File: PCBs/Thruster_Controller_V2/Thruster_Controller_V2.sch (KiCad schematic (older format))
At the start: 33 parts, among them J1 PHASE_A, J2 PHASE_B, J3 PHASE_C, J4 Conn_01x01, J5 Pogo Conn, J6 Conn_01x01, J7 Conn_01x01, J8 Conn_01x01, U4 TPS62172DSGR, U8 MCP2562, Y1 20MHz

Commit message: Powertrain Schematic
- Updated PT schematic, footprints, and part numbers.
- Big change is moving from the DRV8305 to the DRV8320S
- BIG space and cost savings!!
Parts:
- removed C21, C22: 15pF, Capacitors_SMD:C_0402, symbol Device:C_Small
- removed C29: 1uF, Capacitors_SMD:C_0603, symbol Device:C_Small
- removed C30, C42: 0.1uF, Capacitors_SMD:C_0402, symbol Device:C_Small
- removed C49: 10uF, Capacitors_SMD:C_0805, symbol Device:C_Small
- removed C50: 22uF, Capacitors_SMD:C_0805, symbol Device:C_Small
- removed H1, H2: MountingHole, Thruster_Controller:MountingHole_M2, symbol Mechanical:MountingHole
- removed L1: 2.2uH, Inductors_SMD:L_0805, symbol Device:L_Small
- removed R17: 10k, Resistors_SMD:R_0402, symbol Device:R_Small_US
- removed R23: 100k, Resistors_SMD:R_0402_NoSilk, symbol Device:R_Small_US
- removed TP2: TestPoint, Thruster_Controller:TestPoint_Pad_D1.0mm, symbol Connector:TestPoint
- removed U4: TPS62172DSGR, Thruster_Controller:8-Pin_WSON, symbol Thruster_Controller:TPS62172DSGR
- removed Y1: 20MHz, Crystals:Crystal_SMD_SeikoEpson_TSX3225-4pin_3.2x2.5mm, symbol Device:Crystal_GND24
- added C?: 1uF, Capacitors_SMD:C_0603, symbol Device:C_Small
- added C?: 1uF, Capacitors_SMD:C_0805, symbol Device:C_Small
- added U?: NCP718AMT330, Housings_DFN_QFN:DFN-6-1EP_2x2mm_Pitch0.65mm, symbol Thruster_Controller:NCP718AMT330
- R19: footprint Resistors_SMD:R_0805 -> Resistors_SMD:R_0603; Digikey 2019-RK73B2ATTD331JCT-ND -> RMCF0603JT330RCT-ND
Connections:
- net labels removed: +5V
- wire segments 156 -> 99
- no-connect marks 1 -> 0
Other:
- note added: "3.3V Linear Regulator"
- note removed: "3.3V Regulator"
- note removed: "CAN chips decoupling cap"
- moved on the sheet: C23, C28, D1, D3, J4, J6, R19, R35, R7, TP1, TP3, U8

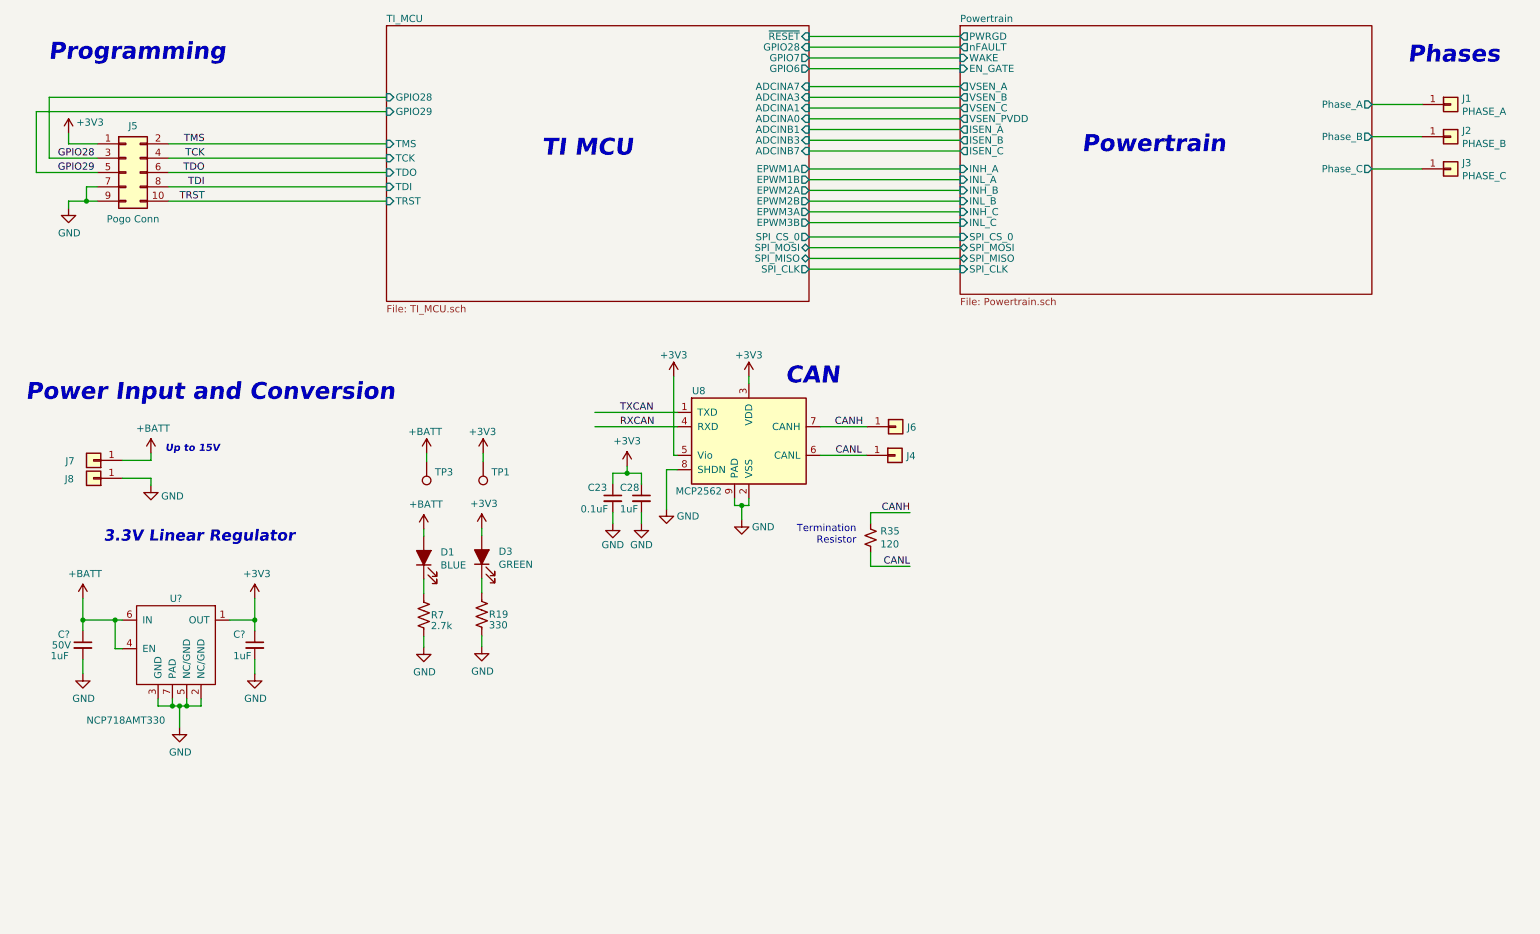
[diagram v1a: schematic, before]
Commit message: Schematic V1
- Completed New Schematic
_ Multiplexed all required signals, may need to redo some arrangments to aid in routing, just because I can and already have to reassign all pins in the SW.
- Created new BOM, only $1 more expensive per board, still might be able to lower that further.
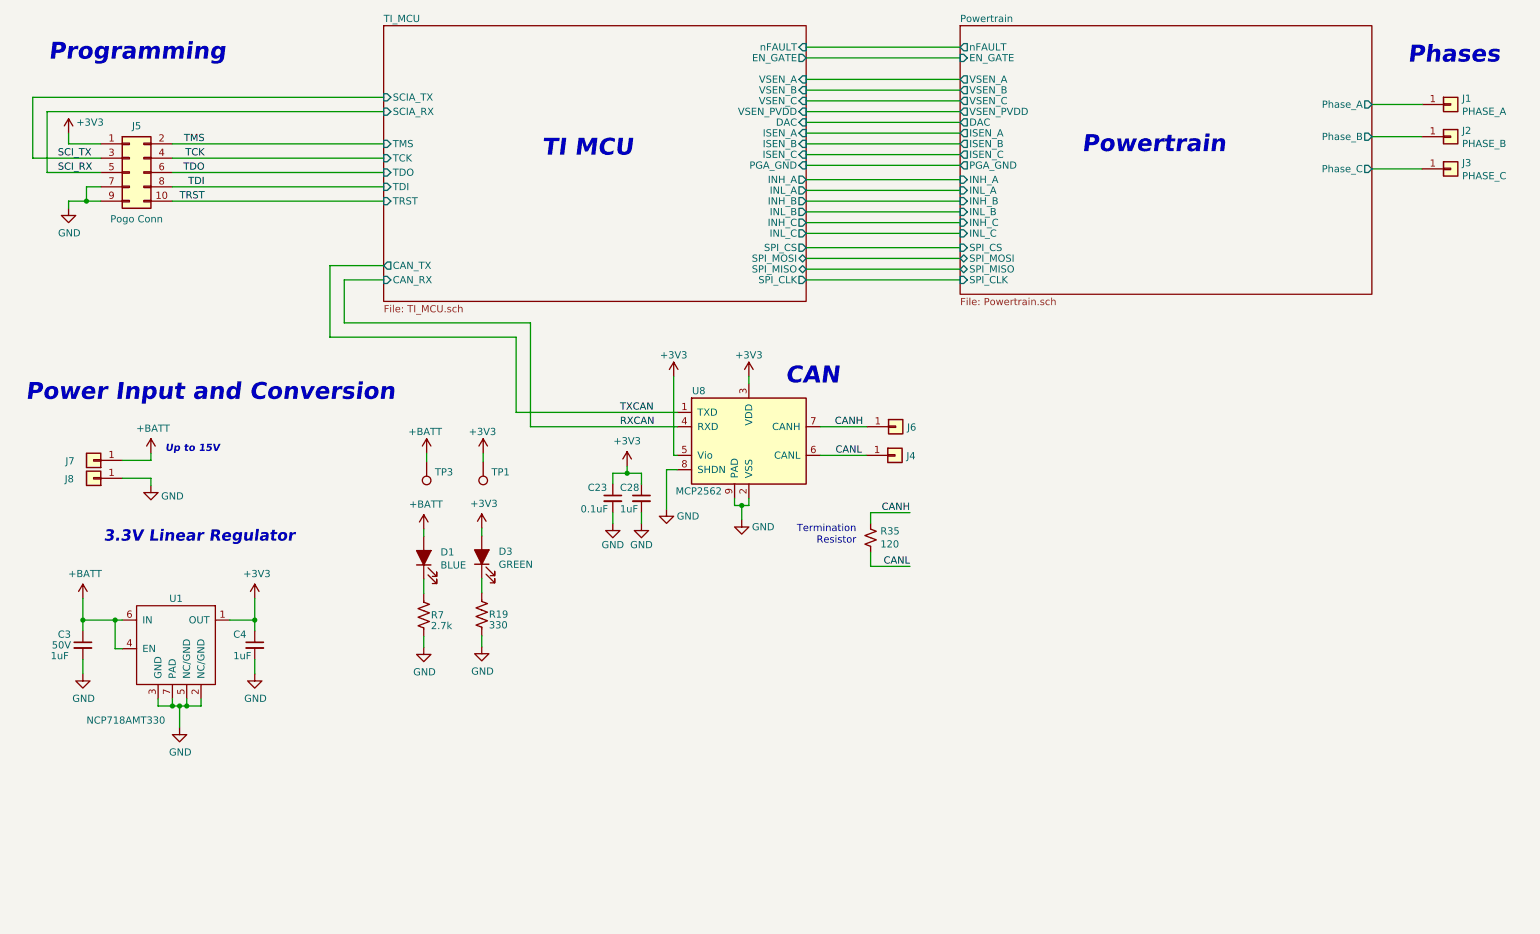
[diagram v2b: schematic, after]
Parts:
- gave numbers to parts that had none: 3
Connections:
- net GPIO28 renamed SCI_TX
- net GPIO29 renamed SCI_RX
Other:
- moved on the sheet: J5

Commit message: Schematic Work / BOM
- Double checking pinout
- Adding digikey PNs for all components, cannot do a mouser run for a small quantity (1-2 boards)
- Generated BOM
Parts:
- R19: value 330 -> 180; Digikey RMCF0603JT330RCT-ND -> 2019-RK73B1JTTD181JCT-ND
- U1: Digikey (none) -> NCP718AMT330TBGOSCT-ND
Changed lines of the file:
@@
 Sheet 1 3
 Title "FOC Thruster Controller "
-Date "2020-05-04"
+Date "2020-08-22"
 Rev "V2"
 Comp "Mark Belbin"
@@
 Text Notes 10300 1725 0    118  Italic 24
 Phases
-Text Notes 1195 5065 0    79   Italic 16
+Text Notes 1050 5125 0    79   Italic 16
 3.3V Linear Regulator
 Wire Wire Line
@@
 F 2 "Housings_DFN_QFN:DFN-6-1EP_2x2mm_Pitch0.65mm" H 1675 5600 50  0001 C CNN
 F 3 "https://www.mouser.ca/datasheet/2/308/NCP718-D-1224359.pdf" H 1625 5400 50  0001 C CNN
-F 4 "" H 1675 5750 50  0001 C CNN "Digikey"
+F 4 "NCP718AMT330TBGOSCT-ND" H 1675 5750 50  0001 C CNN "Digikey"
 F 5 "863-NCP718AMT330TBG" H 1675 5750 50  0001 C CNN "Mouser"
 	1    1675 5750
@@
 AR Path="/5E5672C2" Ref="R19"  Part="1"
 F 0 "R19" H 3885 5560 50  0000 L CNN
-F 1 "330" H 3885 5485 50  0000 L CNN
+F 1 "180" H 3885 5485 50  0000 L CNN
 F 2 "Resistors_SMD:R_0603" V 3875 5550 50  0001 C CNN
 F 3 "~" H 3835 5560 50  0001 C CNN
-F 4 "RMCF0603JT330RCT-ND" H 3835 5560 50  0001 C CNN "Digikey"
+F 4 "2019-RK73B1JTTD181JCT-ND" H 3835 5560 50  0001 C CNN "Digikey"
 	1    3835 5560
 	1    0    0    -1

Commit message: 3V3 LED
- Decreased in series resistor to 100 ohms from 180
- This increased brightness of the LED nicely, which is important to get through clear epoxy.
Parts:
- R19: value 180 -> 100; Digikey 2019-RK73B1JTTD181JCT-ND -> 2019-RK73B1JTTD101JCT-ND
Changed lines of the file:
@@
 AR Path="/5E5672C2" Ref="R19"  Part="1"
 F 0 "R19" H 3885 5560 50  0000 L CNN
-F 1 "180" H 3885 5485 50  0000 L CNN
+F 1 "100" H 3885 5485 50  0000 L CNN
 F 2 "Resistors_SMD:R_0603" V 3875 5550 50  0001 C CNN
 F 3 "~" H 3835 5560 50  0001 C CNN
-F 4 "2019-RK73B1JTTD181JCT-ND" H 3835 5560 50  0001 C CNN "Digikey"
+F 4 "2019-RK73B1JTTD101JCT-ND" H 3835 5560 50  0001 C CNN "Digikey"
 	1    3835 5560
 	1    0    0    -1

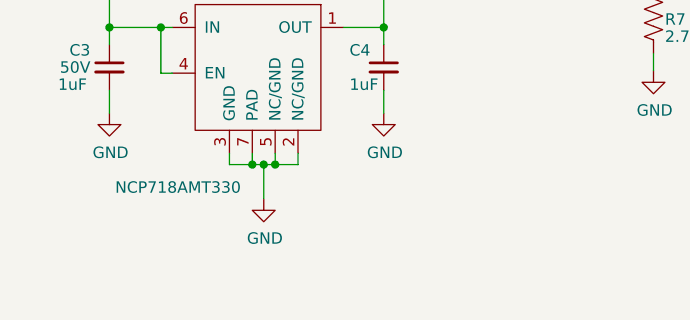
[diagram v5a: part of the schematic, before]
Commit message: Started CAN updates
- Need to fix CAN transciever, add 5V rail!
- Also subbing in a new transciever that is a newer PN and is lower in cost.
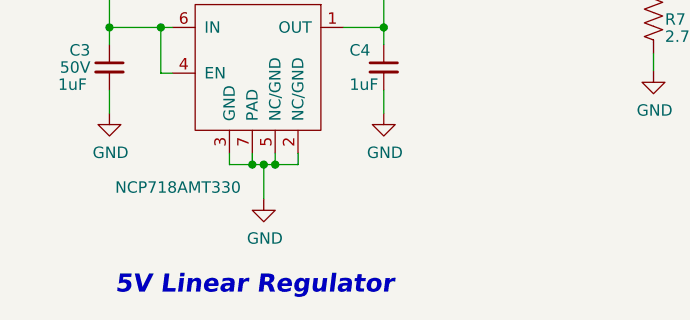
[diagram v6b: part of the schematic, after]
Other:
- note added: "5V Linear Regulator"
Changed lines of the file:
@@
 Wire Wire Line
 	4175 4250 5200 4250
+Text Notes 1075 6775 0    79   Italic 16
+5V Linear Regulator
 $EndSCHEMATC

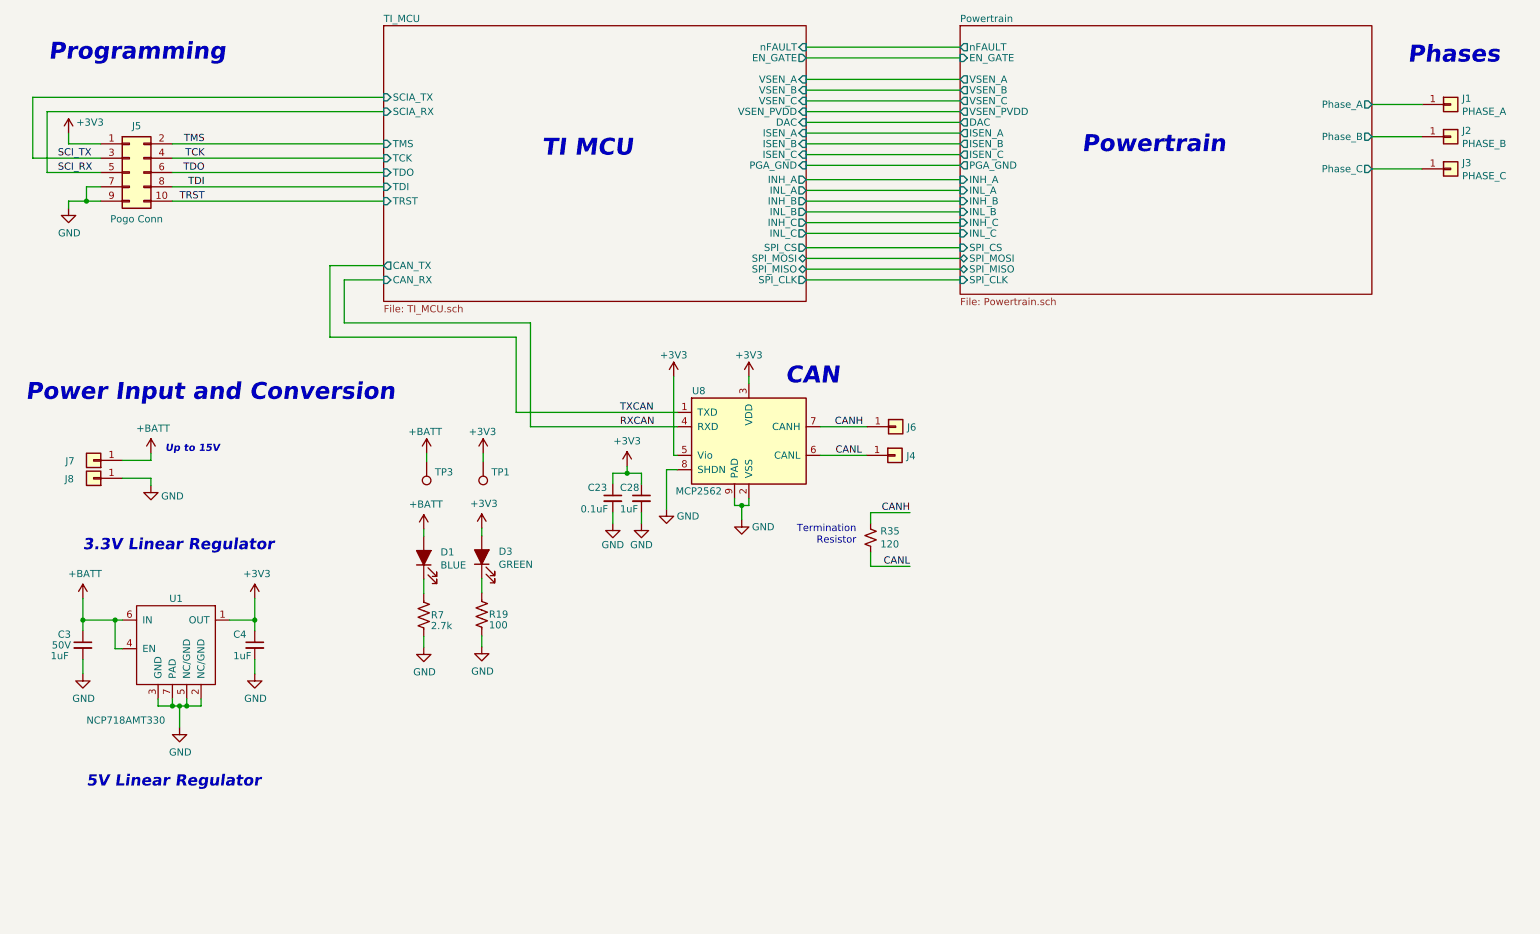
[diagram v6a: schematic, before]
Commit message: Schematic Changes
- Added 5V LDO
- Added 5V LED indicator
- Added 5V testpad
- Changed CAN Transciever to a cheaper and newer model.
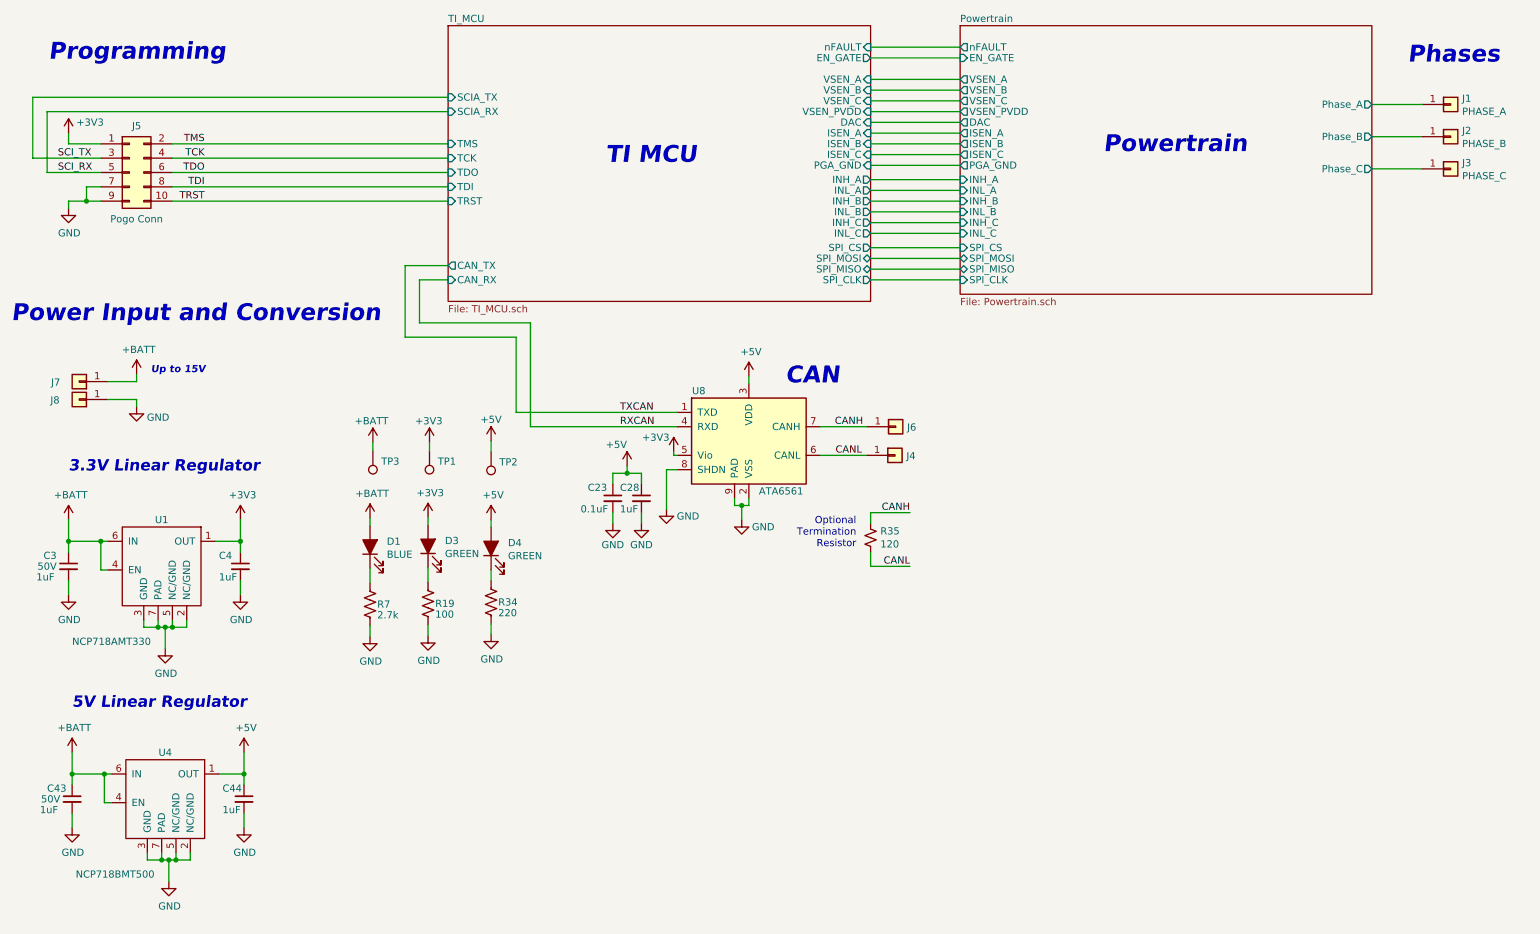
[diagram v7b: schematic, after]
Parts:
- added C43: 1uF, Capacitors_SMD:C_0805, symbol Device:C_Small
- added C44: 1uF, Capacitors_SMD:C_0603, symbol Device:C_Small
- added D4: GREEN, LEDs:LED_0603, symbol Device:LED_ALT
- added R34: 220, Resistors_SMD:R_0603, symbol Device:R_US
- added TP2: TestPoint, Thruster_Controller:TestPoint_Pad_D1.0mm, symbol Connector:TestPoint
- added U4: NCP718BMT500, Housings_DFN_QFN:DFN-6-1EP_2x2mm_Pitch0.65mm, symbol Thruster_Controller:NCP718AMT330
- U8: value MCP2562 -> ATA6561; Digikey MCP2562-E/MF-ND -> ATA6561-GBQW-NCT-ND; Mouser (none) -> 579-ATA6561-GBQW-N
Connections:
- net +3V3: no longer C23.1, C28.1, U8.3 (VDD)
- net +BATT: now also C43.1, U4.4 (EN), U4.6 (IN)
- net GND: now also C43.2, C44.2, R34.2, U4.2 (NC/GND), U4.3 (GND), U4.5 (NC/GND), U4.7 (PAD)
- new net: D4.1 (K), R34.1
- new net +5V: C23.1, C28.1, C44.1, D4.2 (A), TP2.1, U4.1 (OUT), U8.3 (VDD)
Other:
- note added: "Optional\nTermination\nResistor"
- note removed: "Termination\nResistor"
- moved on the sheet: C3, C4, D1, D3, J7, J8, R19, R7, TP1, TP3, U1
